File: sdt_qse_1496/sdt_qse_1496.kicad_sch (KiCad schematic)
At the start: 118 parts, among them J1 SJ-3524-SMT, J2 RF2-04A-T-00-50-G, J3 Conn_01x02_Male, J4 Conn_02x08_Odd_Even, J5 RF2-04A-T-00-50-G, Q1 Q_NPN_BEC, Q2 Q_NPN_BEC, Q3 Q_PMOS_GSD, Q4 Q_PMOS_GSD, T1 Transformer_SP_1S, U1 SN74AC74PW, U2 MC1496DR2G, U3 MC1496DR2G, U4 MC1496DR2G, U5 MC1496DR2G

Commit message: Layout mostly done.  In review.
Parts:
- removed C10, C13, C18, C21, C5, C9: 25uF 25V, symbol Device:C_Polarized_Small
- removed C14, C16, C22, C24: 0.1uF, symbol Device:C_Small
- removed J2, J5: RF2-04A-T-00-50-G, CONN_RF2-04A-T-00-50-G_ADM, symbol SMA_Conn_SMT:RF2-04A-T-00-50-G
- removed R13, R15: 100, symbol Device:R_US
- removed R18, R19, R29, R31, R46, R48: 10k, symbol Device:R_US
- removed R21, R25: 820, symbol Device:R_US
- removed R23, R27: 51, symbol Device:R_US
- removed R33, R36: 1.3k, symbol Device:R_US
- removed R42, R44: 1.0k, symbol Device:R_US
- removed R51, R53, R57, R59: R_US, symbol Device:R_US
- removed RV2, RV4: 50k, symbol Device:R_Potentiometer_US
- removed T1: Transformer_SP_1S, symbol Device:Transformer_SP_1S
- removed U3, U5: MC1496DR2G, SOIC14_4X8P75_ONS, symbol MC1496:MC1496DR2G
- added C10, C5, C9: 0.1uF, Capacitor_SMD:C_1206_3216Metric, symbol Device:C_Small
- added FB1: FerriteBead, Inductor_SMD:L_1206_3216Metric, symbol Device:FerriteBead
- added J3, J4: 5-1814832-1, digikey-footprints:RF_SMA_Vertical_5-1814832-1, symbol dk_Coaxial-Connectors-RF:5-1814832-1
- added U3: Toroidal_Transformer, sdt_qse_1496:Toroidal_Transformer, symbol sde_qse_1496_library:Toroidal_Transformer
- C1, C15, C17, C2, C23, C25, C3, C30, C31, C6, C7: footprint (none) -> Capacitor_SMD:C_1206_3216Metric
- C11, C12, C19, C20, C4, C8: footprint (none) -> Capacitor_THT:CP_Radial_D5.0mm_P2.00mm
- C26, C27, C28, C29: value 25uF 25V -> 100uF 25V; footprint (none) -> Capacitor_THT:CP_Radial_D8.0mm_P3.50mm
- J1: renamed from J4; footprint (none) -> Connector_IDC:IDC-Header_2x08_P2.54mm_Vertical
- J2: renamed from J1; footprint CUI_SJ-3524-SMT -> Stereo_Jack_SMT:CUI_SJ-3524-SMT
- J6: renamed from J3; footprint (none) -> digikey-footprints:PinHeader_1x2_P2.5mm_Drill1.1mm
- Q1, Q2, Q3, Q4: footprint (none) -> Package_TO_SOT_SMD:SOT-23
- R1, R11, R14, R16, R17, R2, R20, R22, R24, R26, R28, R3, R30, R32, R34, R35, R37, R38, R39, R4, R40, R41, R43, R45, R47, R49, R5, R50, R55, R6, R60, R61, R62, R63, R65, R66, R68, R7, R8, R9: footprint (none) -> Resistor_SMD:R_1206_3216Metric
- R10, R12: value 1.0k -> 100; footprint (none) -> Resistor_SMD:R_1206_3216Metric
- R52, R54, R56, R58: value R_US -> 3k; footprint (none) -> Resistor_SMD:R_1206_3216Metric
- R64, R67: value 100 -> 10; footprint (none) -> Resistor_SMD:R_1206_3216Metric
- RV1, RV3: footprint (none) -> Potentiometer_THT:Potentiometer_Bourns_3296W_Vertical
- U1: footprint SOP65P640X120-14N -> SN74AC74PW:SOP65P640X120-14N
- U2, U4: footprint SOIC14_4X8P75_ONS -> MC1496:MC1496DR2G
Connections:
- net 12V: now also C30.1; no longer C30.2, Q3.3 (D), R34.2, R35.2, R45.1, R47.1, R52.1, R54.1, R56.1, R58.1
- net 3_3V_switched: now also C6.1, FB1.2; no longer Q4.3 (D)
- net GND: now also C30.2, C6.2, C10.2, C9.2, J3.1, J4.1, U3.6 (SecondaryB); no longer C30.1
- net LO_NINETY: no longer C2.1
- net LO_ZERO: no longer C6.1
- net at R14.2, R17.1, U2.1 (SIGNALINPUT): now also C8.1; no longer C4.1
- net at R14.1, R22.1, R5.1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: no longer R10.2, R6.1
- net at C11.1, R30.1, R5.2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: no longer R6.2
- net at R56.2, U2.12 (OUTPUT): now also C2.1
- net at R66.2, R68.2: now also J4.2
- net at R11.2, R16.1, R26.1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: no longer R12.2, R8.1
- net at C12.1, R32.1, R7.2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: no longer R8.2
- net at C7.2, R28.2, U4.10 (CARRIERINPUT): no longer C6.2
- net at C3.2, R24.2, U2.10 (CARRIERINPUT): no longer C2.2
- net at R16.2, R20.1, U4.1 (SIGNALINPUT): now also C4.1; no longer C8.1
- net at R58.2, U4.12 (OUTPUT): now also C5.1
- net at R65.2, R66.1: now also U3.5 (SecondaryA)
- net at R63.2: now also R10.2, U3.2 (Primary1b); no longer R62.2
- net at C1.1: now also J3.2
- new net: C2.2, R6.1
- new net: R12.2, R6.2, U3.3 (Primary2a)
- new net: C10.1, FB1.1, Q4.3 (D)
- new net: R8.2, U3.1 (Primary1a)
- new net: R62.2, U3.4 (Primary2b)
- new net: C5.2, R8.1
- new net 12Vswitched: C9.1, Q3.3 (D), R34.2, R35.2, R45.1, R47.1, R52.1, R54.1, R56.1, R58.1
- no-connect marks 8 -> 6
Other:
- note added: "TXRX"
- moved on the sheet: C26, C30, C4, C8, R1, R2, R3, R4

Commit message: Released to fab.
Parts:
- added C13, C14: 0.1uF, Capacitor_SMD:C_1206_3216Metric, symbol Device:C_Small
- added R13, R15, R18: 100, Resistor_SMD:R_1206_3216Metric, symbol Device:R_US
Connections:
- net GND: now also C13.2, C14.2, R15.1, R18.2
- net at C4.2, R2.2, R4.1: now also C14.1
- net at R10.2, R63.2, U3.2 (Primary1b): now also R13.2
- net at R12.2, R6.2, U3.3 (Primary2a): now also R13.1
- net at C8.2, R1.2, R3.1: now also C13.1
- net at R8.2, U3.1 (Primary1a): now also R18.1
- net at R62.2, U3.4 (Primary2b): now also R15.2

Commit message: More simulations working.
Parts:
- added Q? (x2): MMBT2222, digikey-footprints:SOT-23-3, symbol dk_Transistors-Bipolar-BJT-Single:MMBT2222LT1G
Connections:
- net 12Vswitched: now also Q?.3 (C); no longer R58.1
- net at R10.2, R13.2, U3.2 (Primary1b): no longer R63.2
- net at R2.1: no longer J2.3
- net at R18.1, U3.1 (Primary1a): no longer R8.2
- net at R54.2, U4.6 (OUTPUT): now also Q?.1 (B); no longer C25.1
- new net: Q?.1 (B), U4.12 (OUTPUT)
- now unconnected: C5.1, R58.2
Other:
- added sheet Double Balanced Modulator (MC1496_dbm.kicad_sch)
- moved on the sheet: C1, C10, C11, C12, C13, C14, C15, C17, C19, C2, C20, C23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

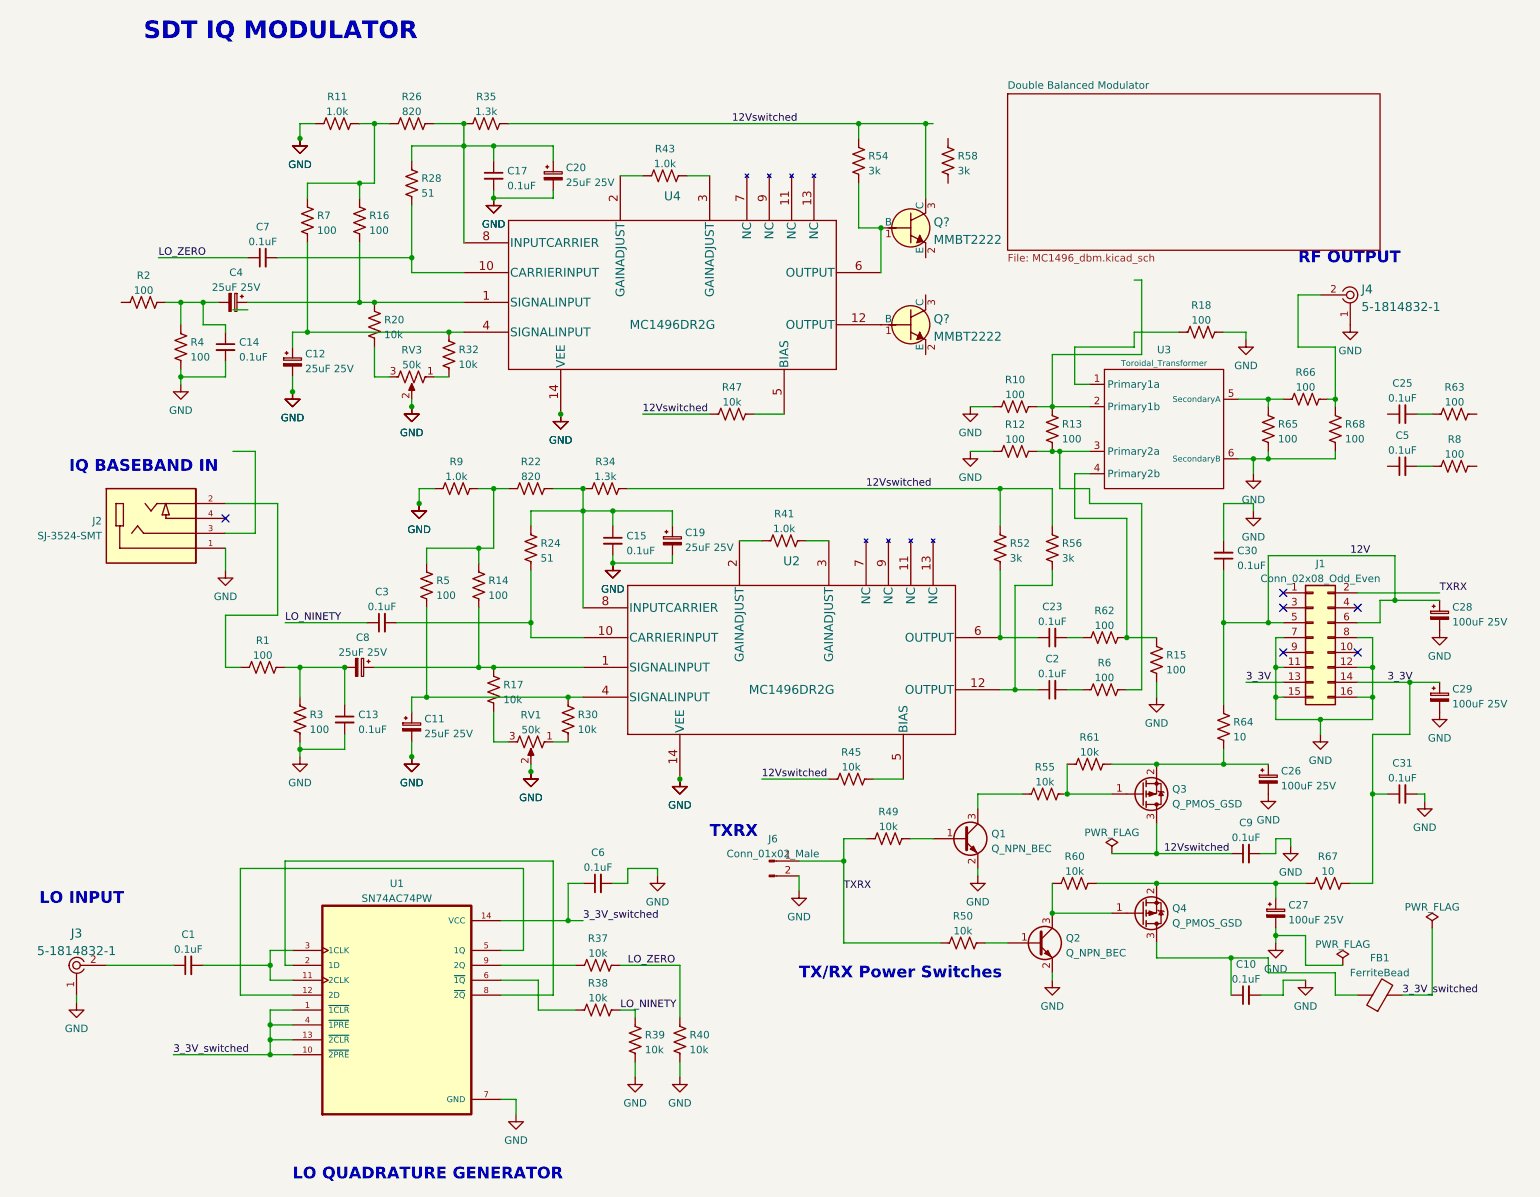
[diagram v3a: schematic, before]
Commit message: Some improvements to the MC1496 simulations.
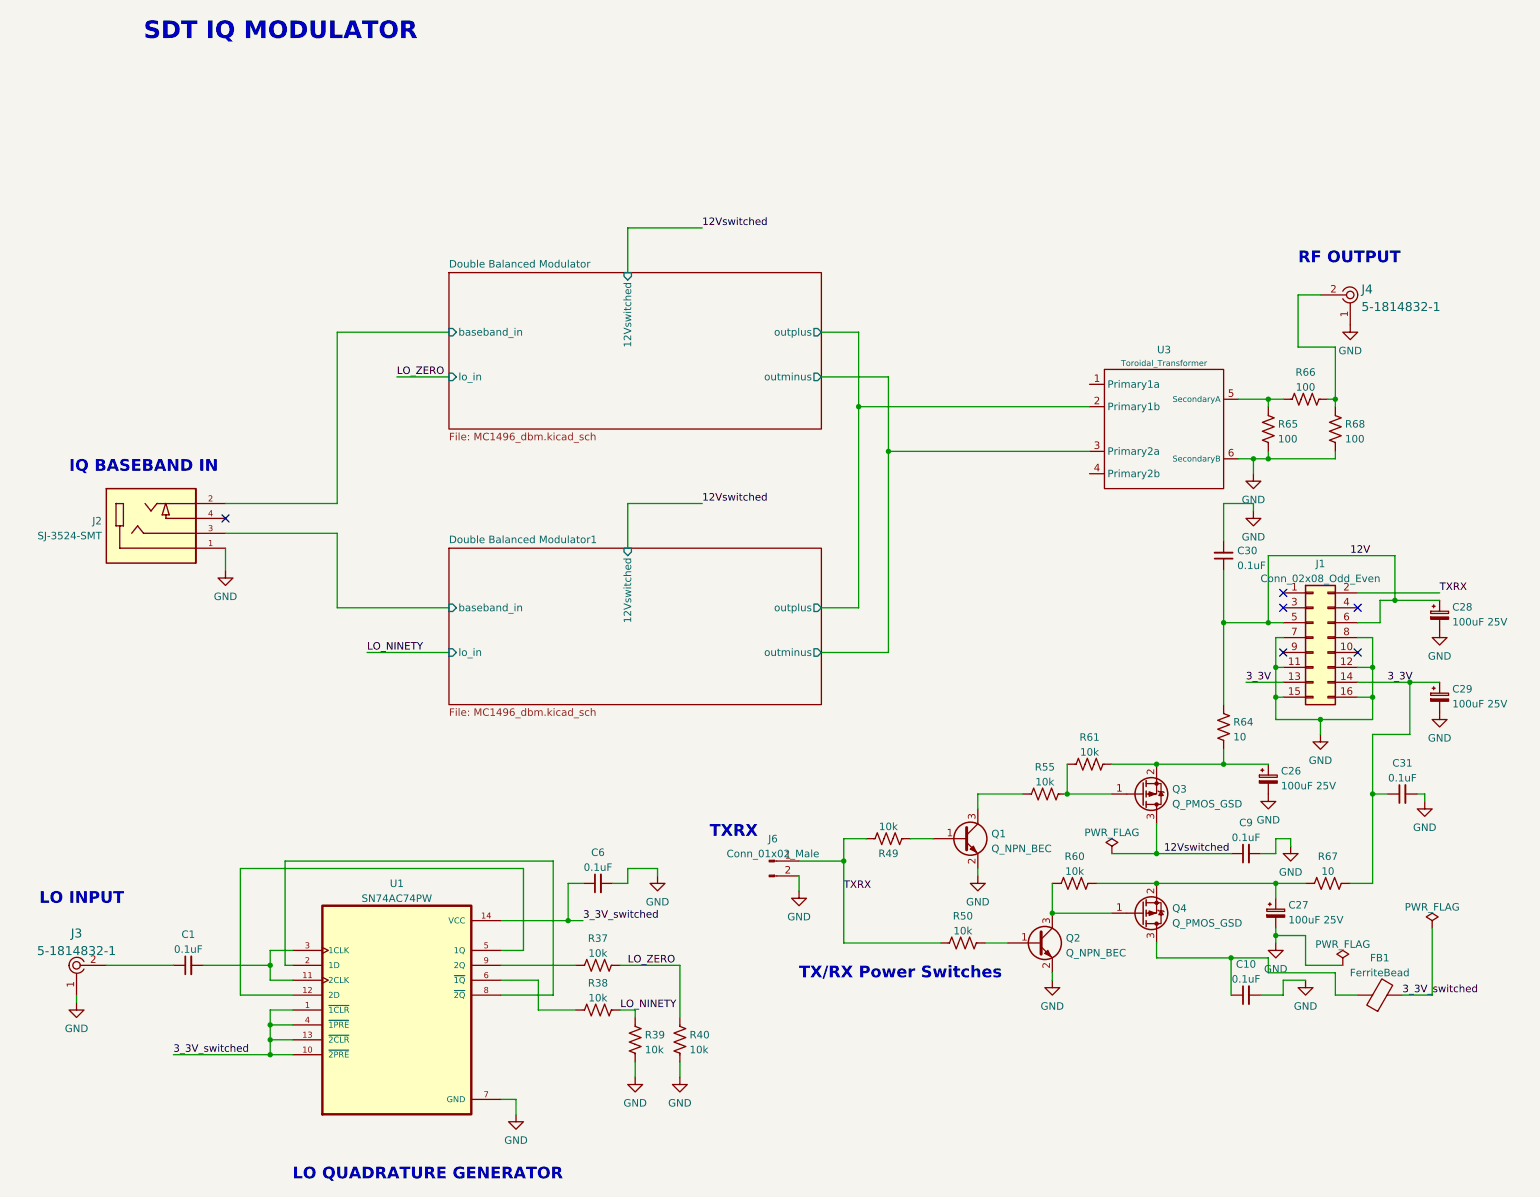
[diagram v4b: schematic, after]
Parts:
- removed C11, C12, C19, C20, C4, C8: 25uF 25V, Capacitor_THT:CP_Radial_D5.0mm_P2.00mm, symbol Device:C_Polarized_Small
- removed C13, C14, C15, C17, C2, C23, C25, C3, C5, C7: 0.1uF, Capacitor_SMD:C_1206_3216Metric, symbol Device:C_Small
- removed Q? (x2): MMBT2222, digikey-footprints:SOT-23-3, symbol dk_Transistors-Bipolar-BJT-Single:MMBT2222LT1G
- removed R1, R10, R12, R13, R14, R15, R16, R18, R2, R3, R4, R5, R6, R62, R63, R7, R8: 100, Resistor_SMD:R_1206_3216Metric, symbol Device:R_US
- removed R11, R41, R43, R9: 1.0k, Resistor_SMD:R_1206_3216Metric, symbol Device:R_US
- removed R17, R20, R30, R32, R45, R47: 10k, Resistor_SMD:R_1206_3216Metric, symbol Device:R_US
- removed R22, R26: 820, Resistor_SMD:R_1206_3216Metric, symbol Device:R_US
- removed R24, R28: 51, Resistor_SMD:R_1206_3216Metric, symbol Device:R_US
- removed R34, R35: 1.3k, Resistor_SMD:R_1206_3216Metric, symbol Device:R_US
- removed R52, R54, R56, R58: 3k, Resistor_SMD:R_1206_3216Metric, symbol Device:R_US
- removed RV1, RV3: 50k, Potentiometer_THT:Potentiometer_Bourns_3296W_Vertical, symbol Device:R_Potentiometer_US
- removed U2, U4: MC1496DR2G, MC1496:MC1496DR2G, symbol MC1496:MC1496DR2G
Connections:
- net Double Balanced Modulator/outplus: now reaches U3.2 (Primary1b)
- net Double Balanced Modulator/outminus: now reaches U3.3 (Primary2a)
- net Double Balanced Modulator/baseband_in: now reaches J2.2
- net Double Balanced Modulator1/baseband_in: now reaches J2.3
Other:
- added sheet Double Balanced Modulator1 (MC1496_dbm.kicad_sch)
- sheet Double Balanced Modulator ports: added 12Vswitched, baseband_in, lo_in, outminus, outplus; removed none

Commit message: Finishing layout of version2.
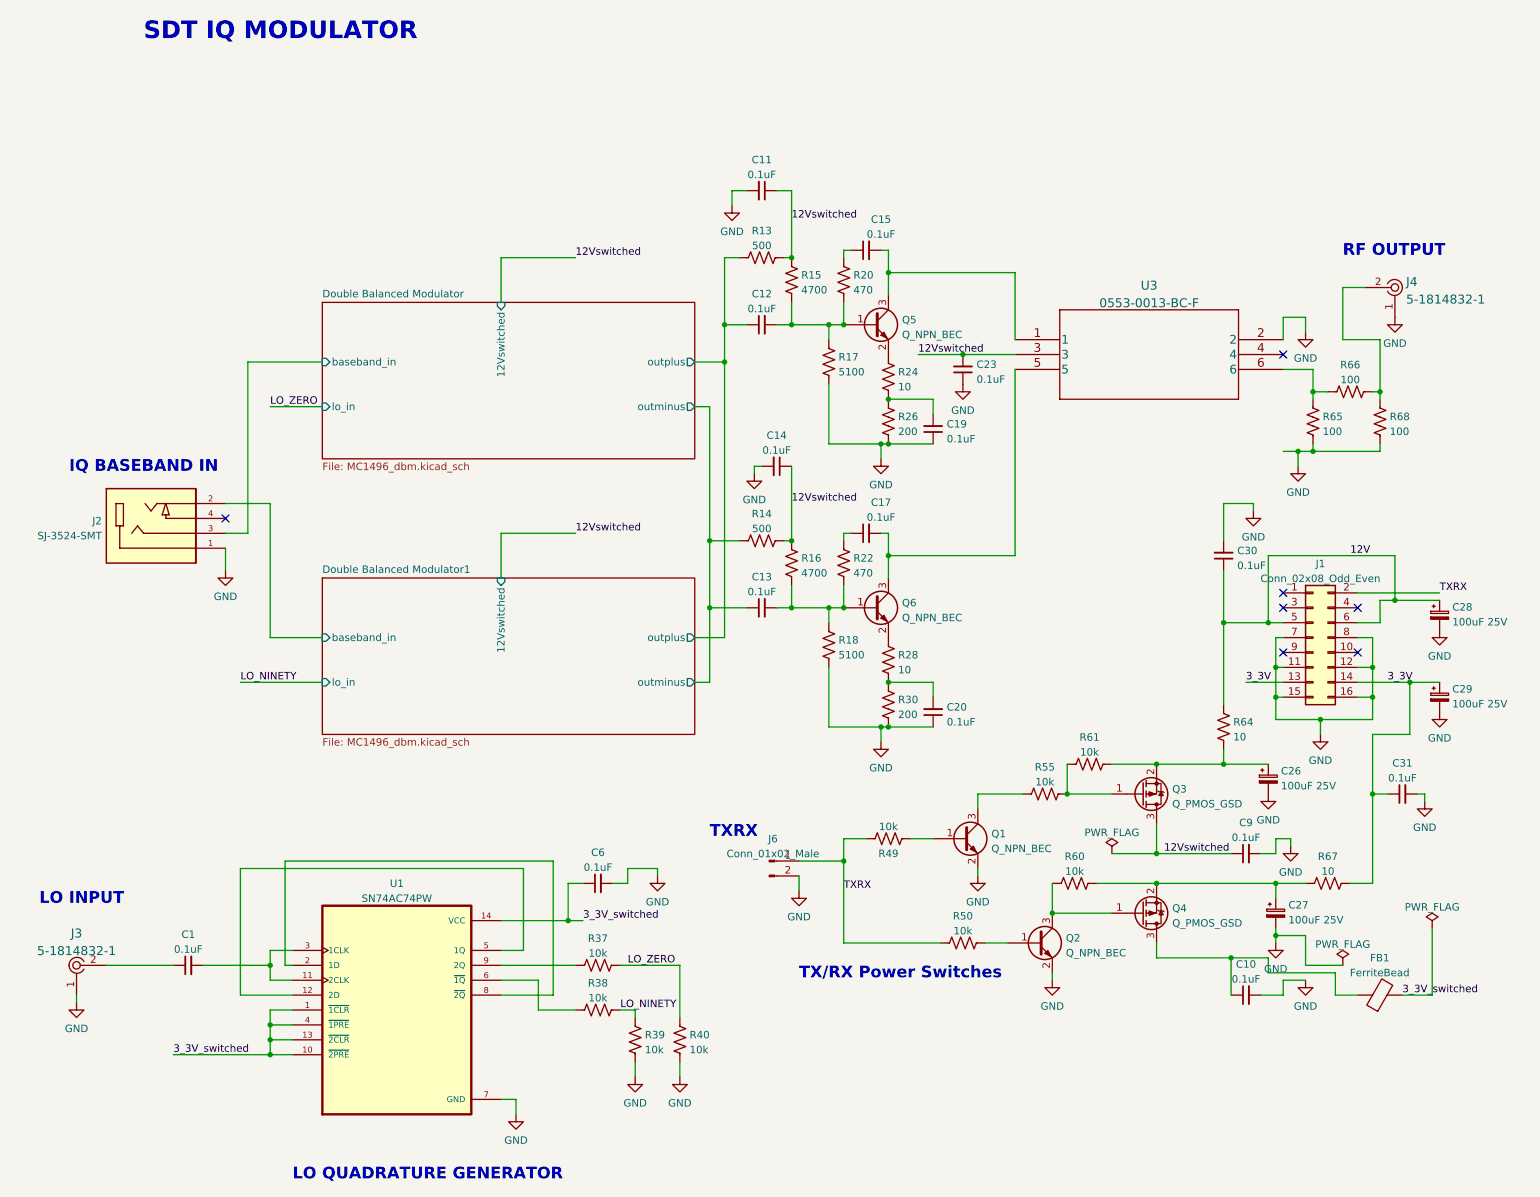
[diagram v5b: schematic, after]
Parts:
- removed U3: Toroidal_Transformer, sdt_qse_1496:Toroidal_Transformer, symbol sde_qse_1496_library:Toroidal_Transformer
- added C11, C12, C13, C14, C15, C17, C19, C20, C23: 0.1uF, Capacitor_SMD:C_1206_3216Metric, symbol Device:C_Small
- added Q5, Q6: Q_NPN_BEC, Package_TO_SOT_SMD:SOT-23, symbol Device:Q_NPN_BEC
- added R13, R14: 500, Resistor_SMD:R_1206_3216Metric, symbol Device:R_US
- added R15, R16: 4700, Resistor_SMD:R_1206_3216Metric, symbol Device:R_US
- added R17, R18: 5100, Resistor_SMD:R_1206_3216Metric, symbol Device:R_US
- added R20, R22: 470, Resistor_SMD:R_1206_3216Metric, symbol Device:R_US
- added R24, R28: 10, Resistor_SMD:R_1206_3216Metric, symbol Device:R_US
- added R26, R30: 200, Resistor_SMD:R_1206_3216Metric, symbol Device:R_US
- added U3: 0553-0013-BC-F, Pulse_Transformer:0553-0013-BC-F, symbol Pulse_Trans_Bell:0553-0013-BC-F
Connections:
- net 12Vswitched: now also C11.1, C14.1, C23.2, R13.1, R14.1, R15.2, R16.2, U3.3
- net Double Balanced Modulator/baseband_in: now also J2.3; no longer J2.2
- net Double Balanced Modulator/outminus: now also C13.1, R14.2
- net Double Balanced Modulator/outplus: now also C12.1, R13.2
- net Double Balanced Modulator1/baseband_in: now also J2.2; no longer J2.3
- net GND: now also C11.2, C14.2, C19.1, C20.1, C23.1, R17.1, R18.1, R26.1, R30.1, U3.2
- net at R65.2, R66.1: now also U3.6
- new net: C19.2, R24.1, R26.2
- new net: Q5.2 (E), R24.2
- new net: C15.1, R20.1
- new net: C12.2, Q5.1 (B), R15.1, R17.2, R20.2
- new net: C15.2, Q5.3 (C), U3.1
- new net: C17.1, R22.1
- new net: C17.2, Q6.3 (C), U3.5
- new net: C20.2, R28.1, R30.2
- new net: C13.2, Q6.1 (B), R16.1, R18.2, R22.2
- new net: Q6.2 (E), R28.2
- no-connect marks 6 -> 7
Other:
- moved on the sheet: J4, R65, R66, R68

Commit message: Added gerbers for Prototype 2.
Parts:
- R37, R38: value 10k -> 470
- R39, R40: value 10k -> 100
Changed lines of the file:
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@@
       (effects (font (size 1.27 1.27)) (justify right))
     )
-    (property "Value" "10k" (id 1) (at 126.111 178.2322 0)
+    (property "Value" "100" (id 1) (at 126.111 178.2322 0)
       (effects (font (size 1.27 1.27)) (justify right))
     )
@@
       (effects (font (size 1.27 1.27)) (justify right))
     )
-    (property "Value" "10k" (id 1) (at 118.491 178.2322 0)
+    (property "Value" "100" (id 1) (at 118.491 178.2322 0)
       (effects (font (size 1.27 1.27)) (justify right))
     )
@@
     (in_bom yes) (on_board yes) (fields_autoplaced)
     (property "Reference" "R38" (id 0) (at 110.49 166.8612 90))
-    (property "Value" "10k" (id 1) (at 110.49 169.3981 90))
+    (property "Value" "470" (id 1) (at 110.49 169.3981 90))
     (property "Footprint" "Resistor_SMD:R_1206_3216Metric" (id 2) (at 110.744 170.434 90)
       (effects (font (size 1.27 1.27)) hide)
@@
     (in_bom yes) (on_board yes) (fields_autoplaced)
     (property "Reference" "R37" (id 0) (at 110.49 159.2412 90))
-    (property "Value" "10k" (id 1) (at 110.49 161.7781 90))
+    (property "Value" "470" (id 1) (at 110.49 161.7781 90))
     (property "Footprint" "Resistor_SMD:R_1206_3216Metric" (id 2) (at 110.744 162.814 90)
       (effects (font (size 1.27 1.27)) hide)
@@
     )
     (path "/f11b2956-7b53-4337-bc68-eec0e1a88425"
-      (reference "R37") (unit 1) (value "10k") (footprint "Resistor_SMD:R_1206_3216Metric")
+      (reference "R37") (unit 1) (value "470") (footprint "Resistor_SMD:R_1206_3216Metric")
     )
     (path "/db00ba08-2f9e-4423-9d6b-a993d9ab40b8"
-      (reference "R38") (unit 1) (value "10k") (footprint "Resistor_SMD:R_1206_3216Metric")
+      (reference "R38") (unit 1) (value "470") (footprint "Resistor_SMD:R_1206_3216Metric")
     )
     (path "/84adc3ef-4e73-43b9-be7b-aa88d78057aa"
-      (reference "R39") (unit 1) (value "10k") (footprint "Resistor_SMD:R_1206_3216Metric")
+      (reference "R39") (unit 1) (value "100") (footprint "Resistor_SMD:R_1206_3216Metric")
     )
     (path "/3f9288f9-2fcb-442f-9dab-330a5e739560"
-      (reference "R40") (unit 1) (value "10k") (footprint "Resistor_SMD:R_1206_3216Metric")
+      (reference "R40") (unit 1) (value "100") (footprint "Resistor_SMD:R_1206_3216Metric")
     )
     (path "/dd6f2fcf-41d2-44f7-ae61-da50c8494c9a/c36cf2c4-337a-419d-abcf-23c70512f7ea"
